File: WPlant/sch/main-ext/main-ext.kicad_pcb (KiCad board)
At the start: 2 copper layers, 159 parts, among them J1 PROG/JTAG, J10 Ext, J11 HSensor, J12 HSensor, J13 HSensor, J14 HSensor, J15 HSensor, J16 HSensor, J17 HSensor, J18 WaterLevel, J2 Battery, J3 Balance, J4 DE9_Receptacle, J5 220V, J6 Conn_01x08_Pin, J8 eInk-Buttons, J9 Leak, M1 Motor_DC, Q1 FDS9926A, Q2 FDS9926A, Q3 FDS9926A, Q4 FDS9926A, Q6 Si2301, Q7 BC817, SW1 SW_Push, SW2 SW_Push, SW3 SW_Push, U1 SIWG917Y121MGABAR, U10 SP485EEN-L/TR, U11 TXU0102QDCURQ1, U12 CD74HCT4051M96, U13 CD74HCT4051M96, U14 SN74LVC1G14DBV, U2 AP64352SP-13, U3 AP64352SP-13, U4 AP64352SP-13, U5 TC4427AEOA713, U6 AP2204R-5.0, U7 74HC594, U8 NC7S02P5, U9 INA180A2, X1 SIT1552AI-JE-DCC-32.768D

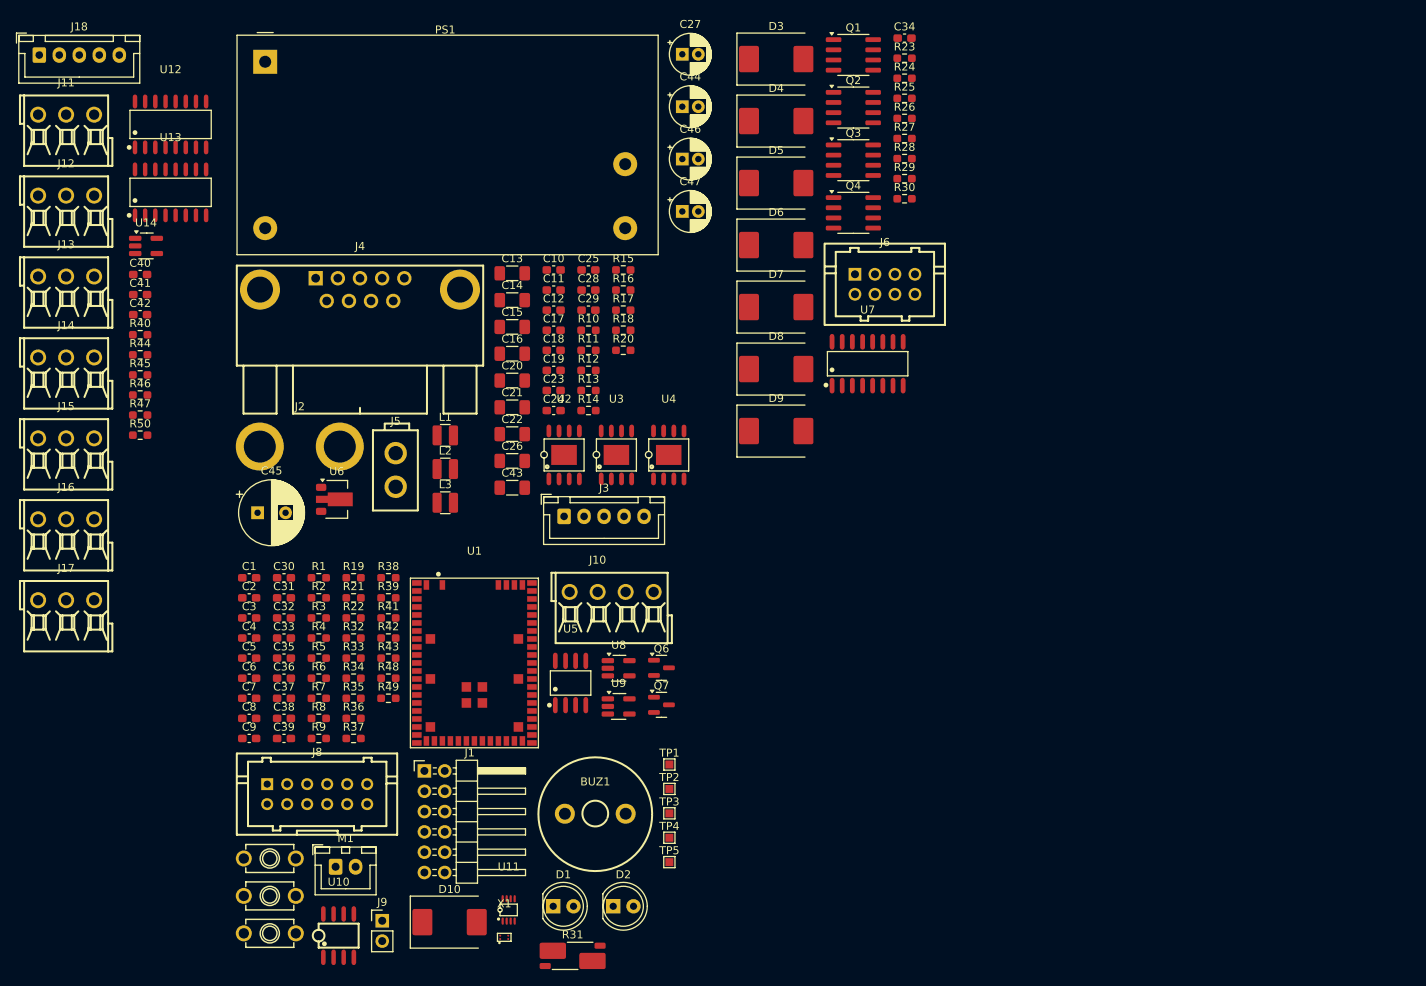
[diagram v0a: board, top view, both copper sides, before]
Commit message: Generic design was splited to Main-Int and Main-Ext
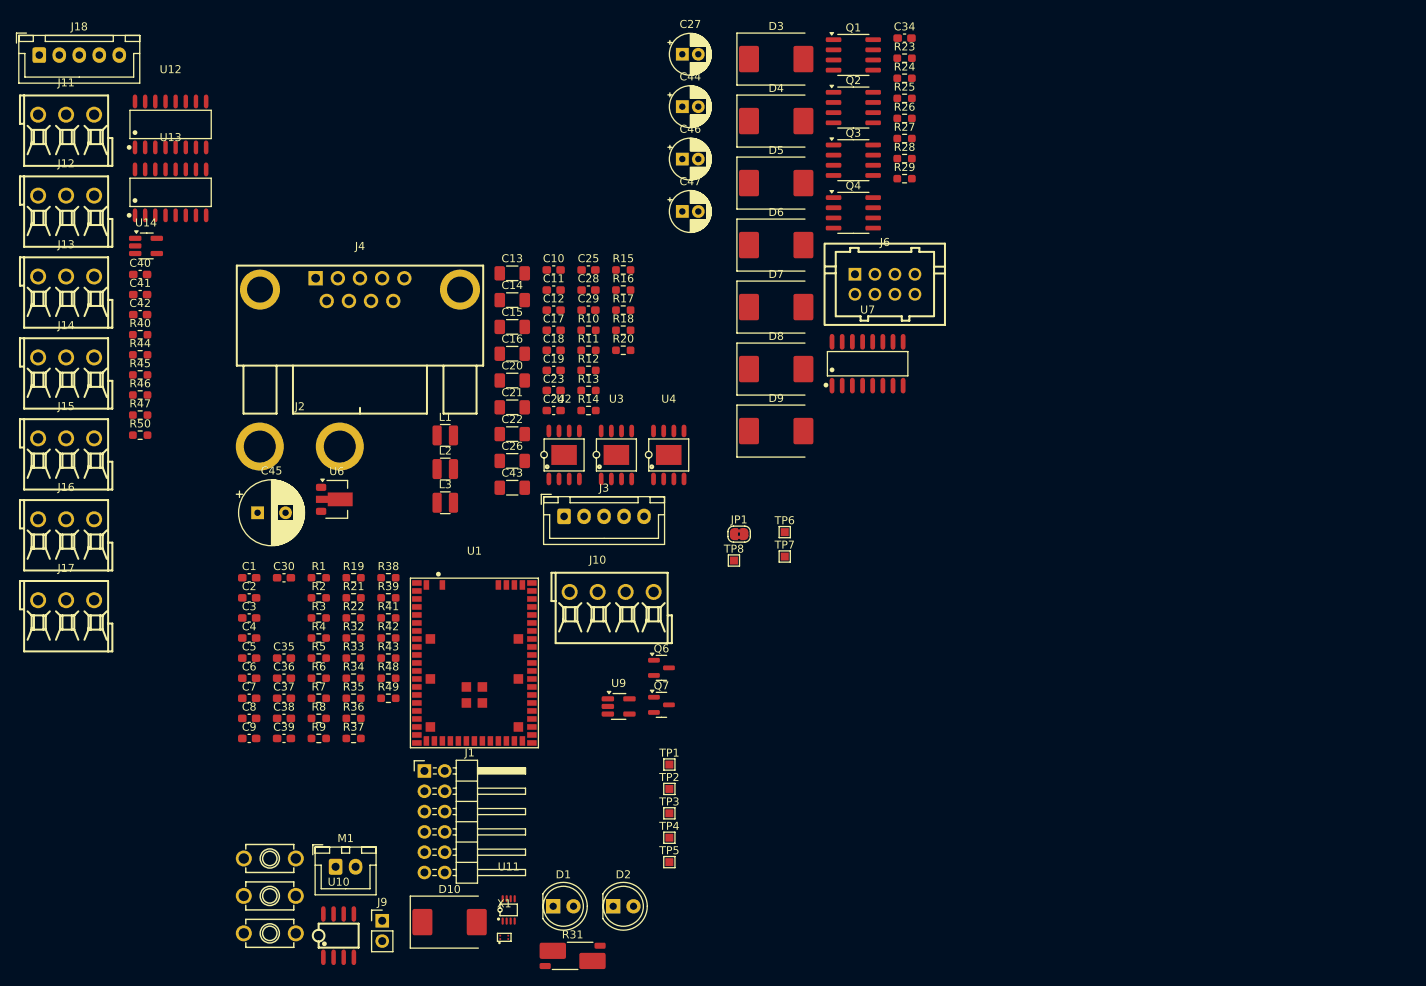
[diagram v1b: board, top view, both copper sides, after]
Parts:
- removed BUZ1: HNR-1407PA7.5, easyeda2kicad:BUZ-TH_BD14.0-P7.60-D0.8-L
- removed C31: 2.2, Capacitor_SMD:C_0603_1608Metric_Pad1.08x0.95mm_HandSolder
- removed C32, C33: 1.0, Capacitor_SMD:C_0603_1608Metric_Pad1.08x0.95mm_HandSolder
- removed J5: 220V, easyeda2kicad:CONN-TH_HAA420A-2A
- removed J8: eInk-Buttons, easyeda2kicad:CONN-TH_XAD-12A
- removed PS1: IRM-20-12, Converter_ACDC:Converter_ACDC_MeanWell_IRM-20-xx_THT
- removed R30: 100, Resistor_SMD:R_0603_1608Metric_Pad0.98x0.95mm_HandSolder
- removed U5: TC4427AEOA713, easyeda2kicad:SOIC-8_L4.9-W3.9-P1.27-LS6.0-BL
- removed U8: NC7S02P5, Package_TO_SOT_SMD:SOT-23-5_HandSoldering
- added JP1: SolderJumper_2_Bridged, Jumper:SolderJumper-2_P1.3mm_Bridged2Bar_RoundedPad1.0x1.5mm, F.Cu at (151.2, 101.6)
- added TP6: TestPoint, TestPoint:TestPoint_Pad_1.0x1.0mm, F.Cu at (156.9, 101.3)
- added TP7: TestPoint, TestPoint:TestPoint_Pad_1.0x1.0mm, F.Cu at (156.9, 104.4)
- added TP8: TestPoint, TestPoint:TestPoint_Pad_1.0x1.0mm, F.Cu at (150.6, 104.9)
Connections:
- net /eInkBusy renamed Net-(U1-ULP_GPIO_1)
- net /eInkCLK renamed /Valves/CLK
- net /eInkDC renamed Net-(U1-GPIO_54)
- net /eInkData renamed /Valves/MOSI
- net /~{eInkCS} renamed /AccSence
- net /~{eInkReset} renamed Net-(U1-GPIO_56)
- Q4 pad 3: /Power/12V -> Net-(JP1-A)
- Q4 pad 5: VBUS -> Net-(Q4B-D2-Pad5)
- Q4 pad 6: VBUS -> Net-(Q4B-D2-Pad5)
- U1 pad 45: /~{BUZZ-EN} -> Net-(U1-GPIO_30)
- U1 pad 47: /BUZZ -> Net-(U1-GPIO_29)

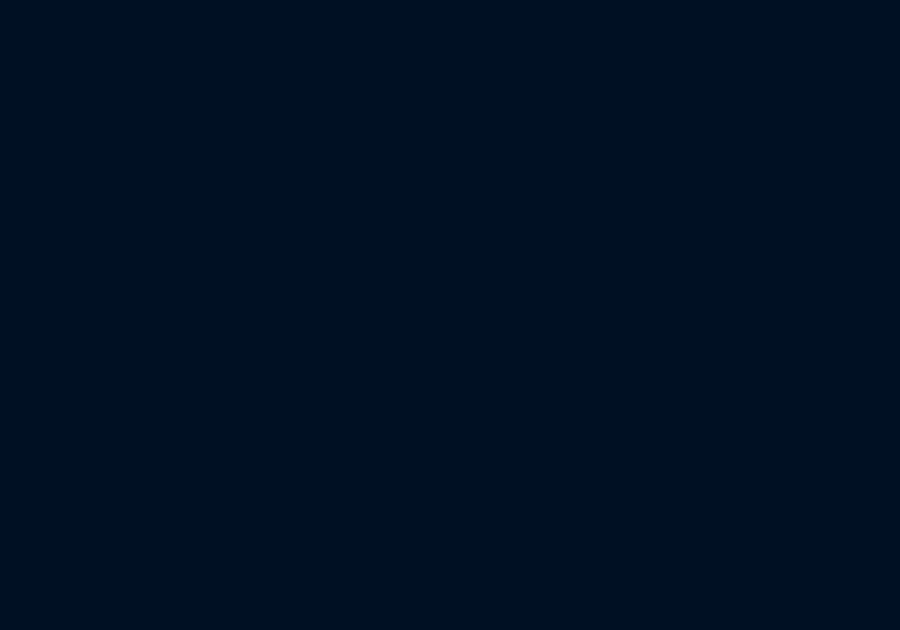
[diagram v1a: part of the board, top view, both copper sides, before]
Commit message: Added jumpers to power lines for Main-* schematics
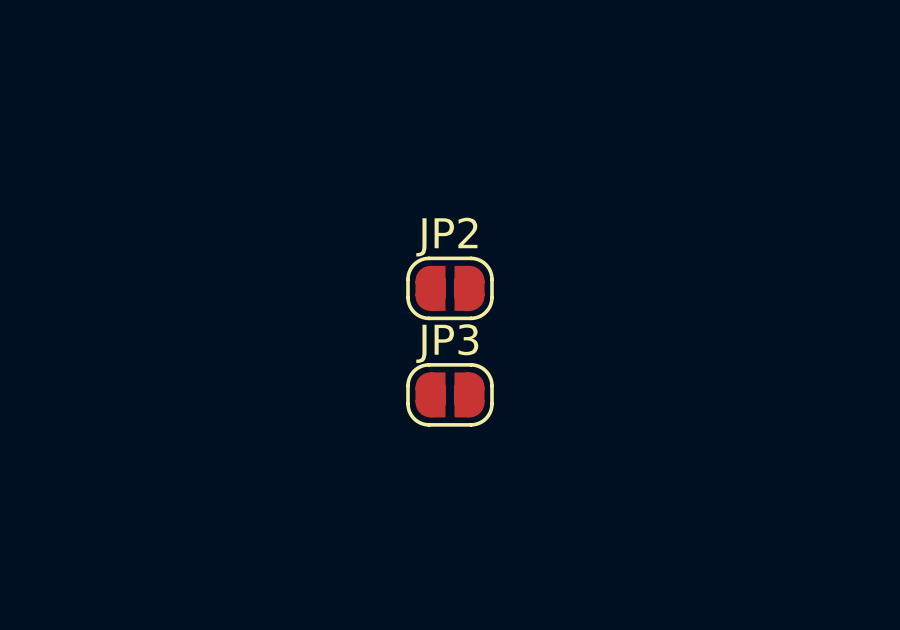
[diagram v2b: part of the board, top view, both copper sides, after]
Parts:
- added JP2: SolderJumper_2_Open, Jumper:SolderJumper-2_P1.3mm_Open_RoundedPad1.0x1.5mm, F.Cu at (109.5, 46.5)
- added JP3: SolderJumper_2_Open, Jumper:SolderJumper-2_P1.3mm_Open_RoundedPad1.0x1.5mm, F.Cu at (109.5, 50.0)
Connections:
- C16 pad 2: +3.3V -> Net-(JP3-A)
- C19 pad 2: +9V -> Net-(JP2-A)
- C20 pad 2: +9V -> Net-(JP2-A)
- C21 pad 2: +9V -> Net-(JP2-A)
- C25 pad 2: +3.3V -> Net-(JP3-A)
- C26 pad 2: +3.3V -> Net-(JP3-A)
- C27 pad 1: +3.3V -> Net-(JP3-A)
- C44 pad 1: +9V -> Net-(JP2-A)
- L2 pad 2: +9V -> Net-(JP2-A)
- L3 pad 2: +3.3V -> Net-(JP3-A)
- R14 pad 1: +9V -> Net-(JP2-A)
- R17 pad 1: +3.3V -> Net-(JP3-A)

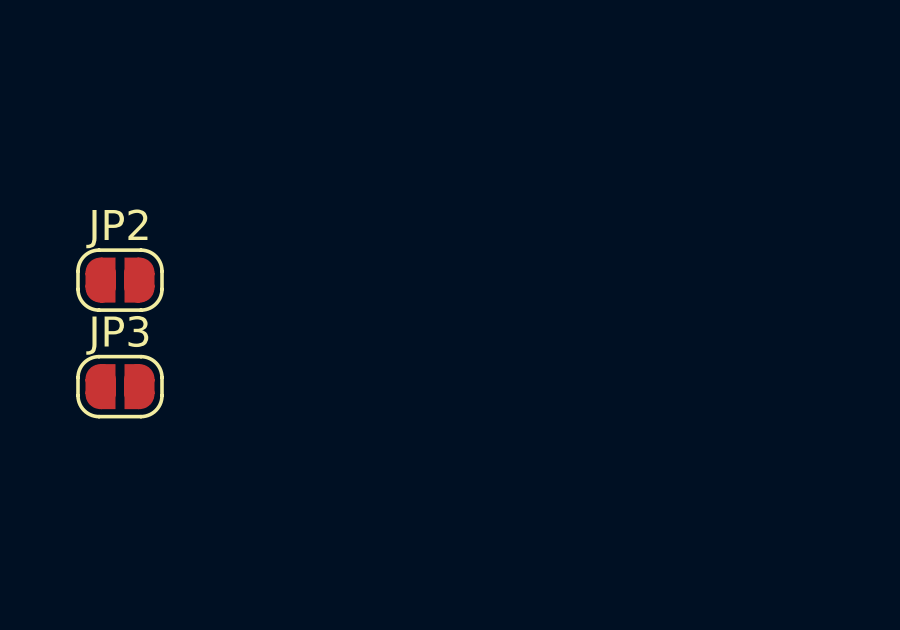
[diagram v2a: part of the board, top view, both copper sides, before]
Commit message: Added more jumpers to power lines for Main-* schematics
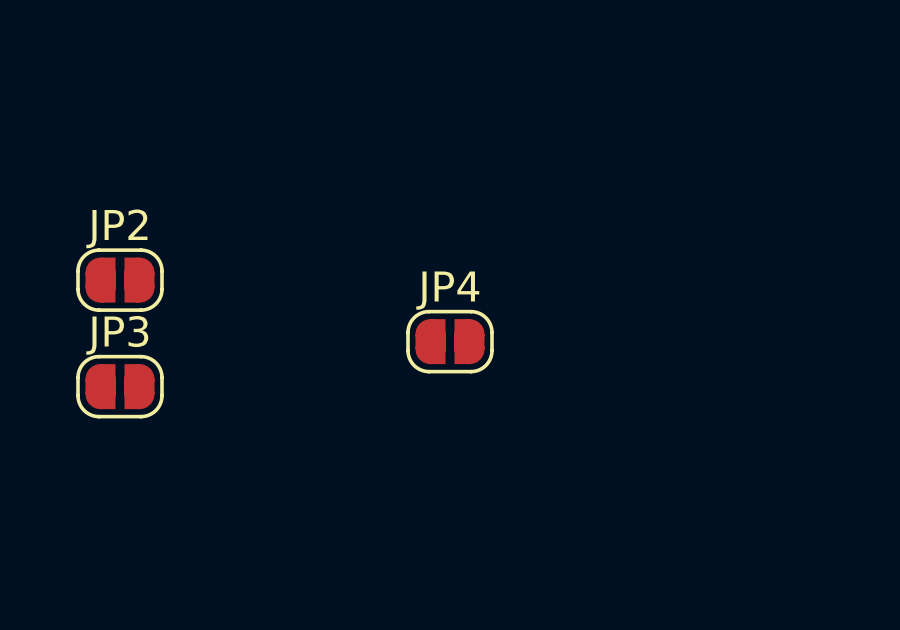
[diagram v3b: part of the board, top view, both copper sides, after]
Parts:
- added JP4: SolderJumper_2_Open, Jumper:SolderJumper-2_P1.3mm_Open_RoundedPad1.0x1.5mm, F.Cu at (120.5, 48.5)
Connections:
- C28 pad 2: +9V -> Net-(JP2-A)
- C29 pad 2: +5V -> Net-(JP4-A)
- C47 pad 1: +5V -> Net-(JP4-A)
- U6 pad 1: +9V -> Net-(JP2-A)
- U6 pad 3: +5V -> Net-(JP4-A)

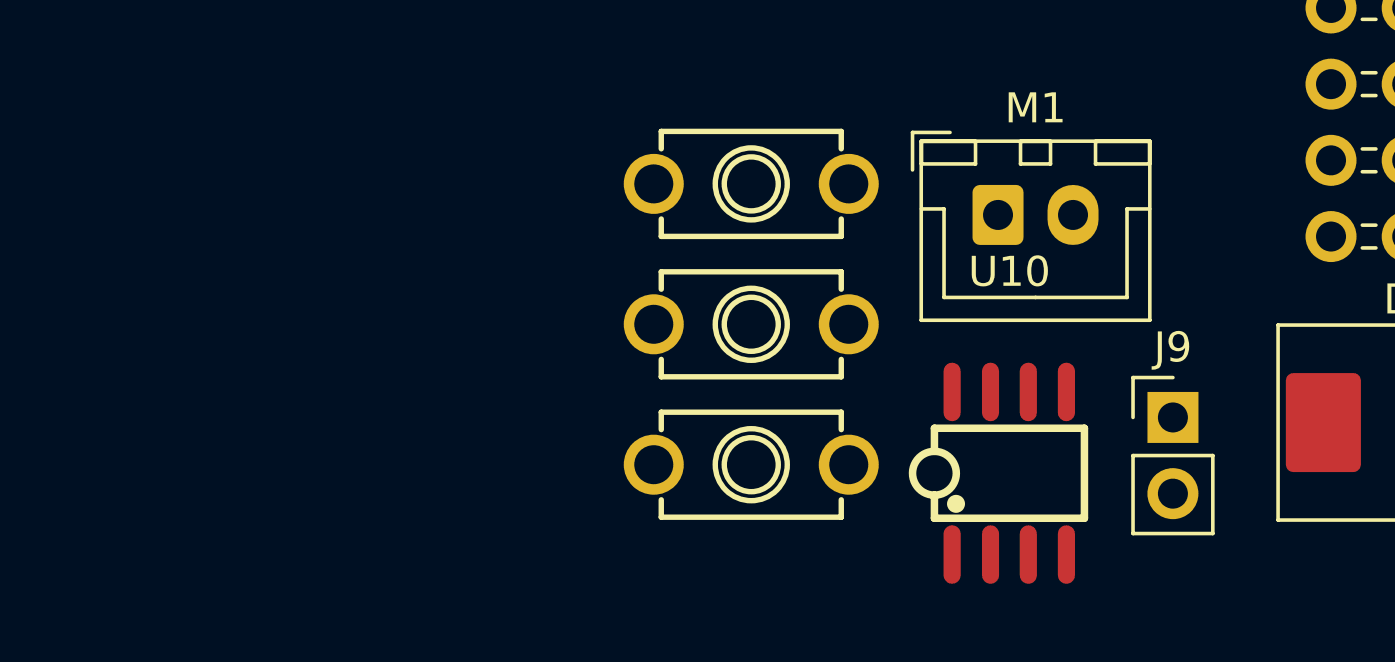
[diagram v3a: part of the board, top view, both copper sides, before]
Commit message: Update SWIG917 footprint. Change footprint of LeakDetector
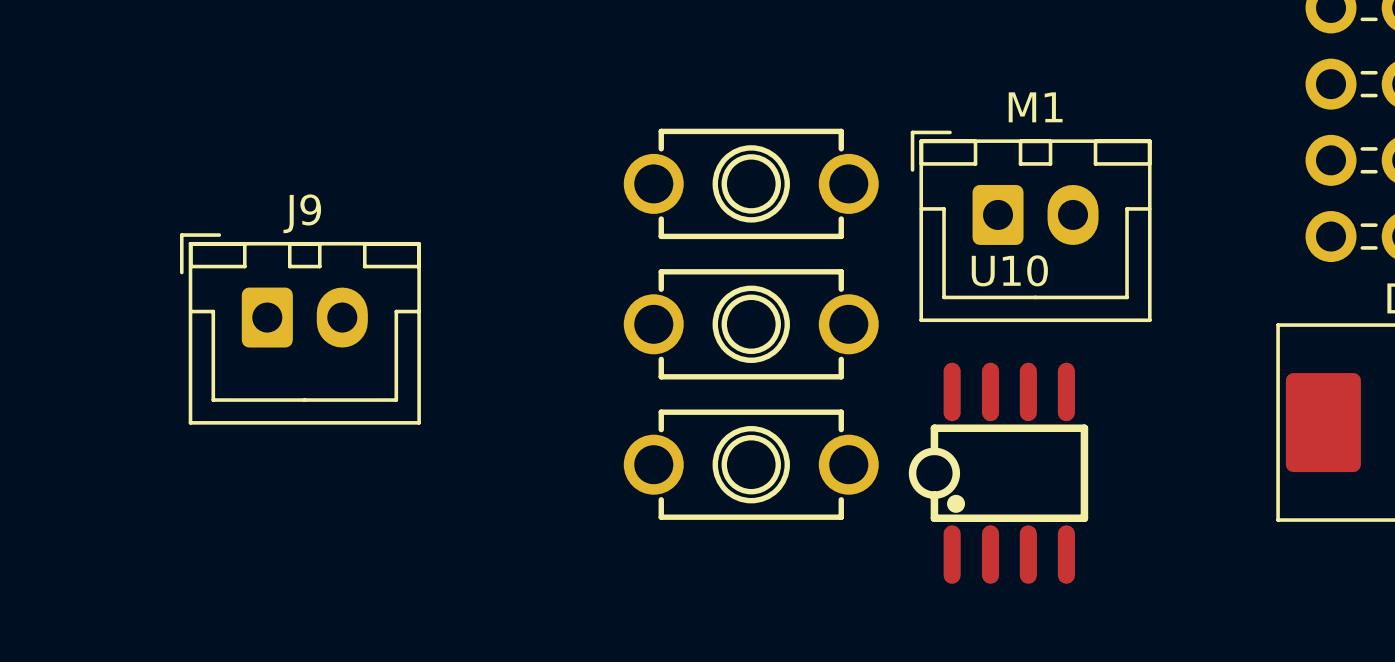
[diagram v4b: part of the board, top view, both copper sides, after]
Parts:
- J9: footprint Connector_PinHeader_2.54mm:PinHeader_1x02_P2.54mm_Vertical -> Connector_JST:JST_XH_B2B-XH-A_1x02_P2.50mm_Vertical
- moved J9 30.4 mm to (76.4, 146.6)
